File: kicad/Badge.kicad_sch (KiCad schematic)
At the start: 24 parts, among them SW1 SW_SPST, U1 LMC555xM

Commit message: outline draft 3
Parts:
- added C3: 100nF, Capacitor_SMD:C_0805_2012Metric_Pad1.18x1.45mm_HandSolder, symbol Device:C
- C1: value C -> 1uF
- R6, R7, R8, R9: value 470 -> 390
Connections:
- net GND: now also C3.2
- net VCC: now also C3.1
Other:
- note added: "3V 20mm coin cell CR2032 holder"
- note added: "LEDs"
- note added: "Power Supply"
- note added: "Timer"
- moved on the sheet: BT1, C1, C2, D1, D2, D3, D4, D5, D6, D7, D8, JP1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

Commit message: routing 1
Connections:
- net PULSE2L: now reaches JP2.2 (C), R6.2, R7.2, R8.2, R9.2
- net PULSE2H: now reaches D5.2 (A), D6.2 (A), D7.2 (A), D8.2 (A), JP1.2 (C)
- net BAT: now reaches BT1.1 (+), SW1.1 (A)
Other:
- company: (none) -> NJIT ECET 430
- title: (none) -> 430 Badge Solder Practice Board
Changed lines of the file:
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@@
 	(generator_version "8.0")
 	(paper "A4")
+	(title_block
+		(title "430 Badge Solder Practice Board")
+		(date "2024-10-02")
+		(rev "1.0")
+		(company "NJIT ECET 430")
+		(comment 1 "Open Source Hardware CC BY-NC-SA 4.0")
+	)
 	(junction
 		(at 219.71 48.26)
@@
 		)
 	)
+	(label "PULSE2L"
+		(at 232.41 85.09 270)
+		(fields_autoplaced yes)
+		(effects
+			(font
+				(size 1.27 1.27)
+				(thickness 0.1588)
+			)
+			(justify right bottom)
+		)
+	)
 	(label "PULSE"
 		(at 196.85 48.26 180)
@@
 		)
 	)
+	(label "BAT"
+		(at 27.94 53.34 0)
+		(fields_autoplaced yes)
+		(effects
+			(font
+				(size 1.27 1.27)
+				(thickness 0.254)
+				(bold yes)
+			)
+			(justify left bottom)
+		)
+	)
 	(label "TR"
 		(at 111.76 48.26 180)
@@
 		)
 	)
+	(label "PULSE2H"
+		(at 232.41 69.85 90)
+		(fields_autoplaced yes)
+		(effects
+			(font
+				(size 1.27 1.27)
+				(thickness 0.1588)
+			)
+			(justify left bottom)
+		)
+	)

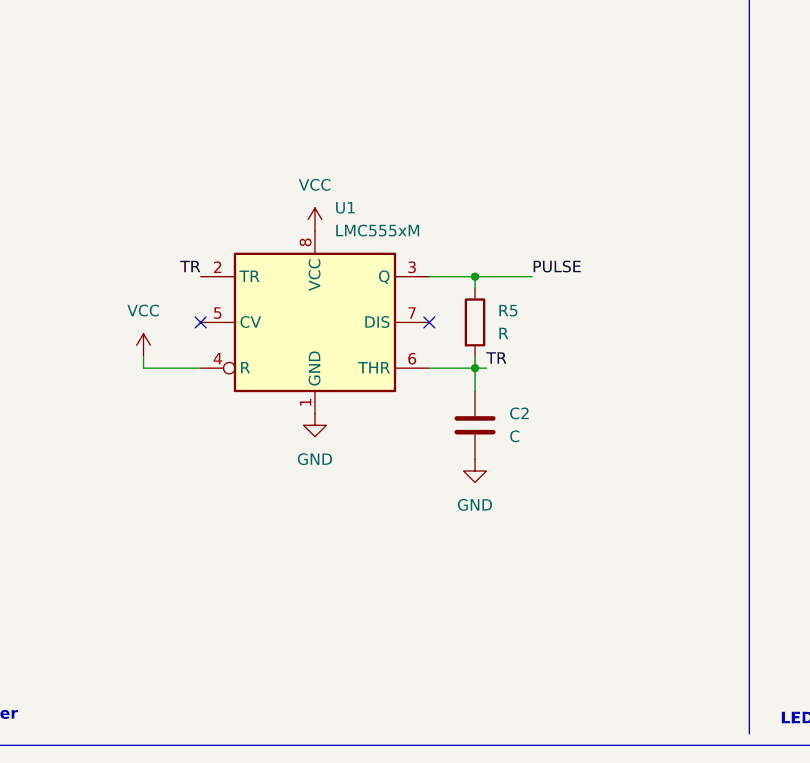
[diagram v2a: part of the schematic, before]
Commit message: fix routing, straight edge sections for solderpaste, milling gerbers
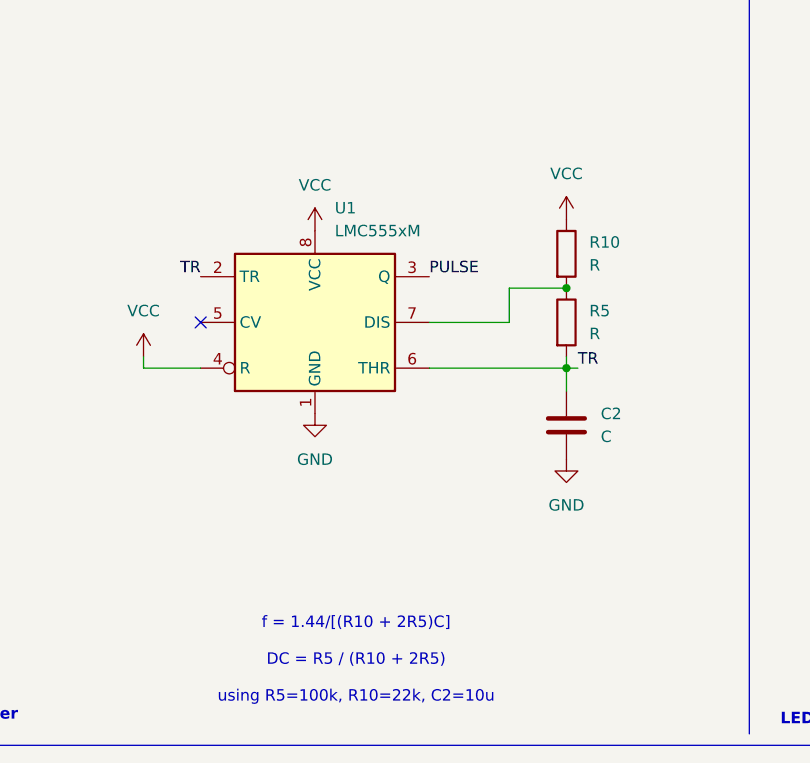
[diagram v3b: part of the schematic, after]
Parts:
- added R10: R, Resistor_SMD:R_0805_2012Metric_Pad1.20x1.40mm_HandSolder, symbol Device:R
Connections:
- net PULSE: no longer R5.1
- net VCC: now also R10.1
- net at U1.7 (DIS): now also R5.1, R10.2
- no-connect marks 2 -> 1
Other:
- note added: "f = 1.44/[(R10 + 2R5)C] DC = R5 / (R10 + 2R5) using R5=100k, R10=22k, C2=10u"
- moved on the sheet: C2, R5
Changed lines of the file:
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@@
 	)
 	(junction
-		(at 142.24 58.42)
+		(at 152.4 58.42)
 		(diameter 0)
 		(color 0 0 0 0)
@@
 	)
 	(junction
-		(at 142.24 48.26)
-		(diameter 0)
-		(color 0 0 0 0)
-	)
-	(junction
 		(at 48.26 63.5)
 		(diameter 0)
@@
 		(color 0 0 0 0)
 	)
-	(no_connect
-		(at 137.16 53.34)
+	(junction
+		(at 152.4 49.53)
+		(diameter 0)
+		(color 0 0 0 0)
 	)
 	(no_connect
@@
 	(wire
 		(pts
-			(xy 142.24 48.26) (xy 148.59 48.26)
-		)
-		(stroke
-			(width 0)
-			(type default)
-		)
-	)
-	(wire
-		(pts
-			(xy 137.16 48.26) (xy 142.24 48.26)
+			(xy 137.16 53.34) (xy 146.05 53.34)
+		)
+		(stroke
+			(width 0)
+			(type default)
+		)
+	)
+	(wire
+		(pts
+			(xy 146.05 49.53) (xy 152.4 49.53)
 		)
 		(stroke
@@
 	(wire
 		(pts
-			(xy 142.24 58.42) (xy 142.24 57.15)
+			(xy 152.4 58.42) (xy 152.4 57.15)
 		)
 		(stroke
@@
 	(wire
 		(pts
-			(xy 137.16 58.42) (xy 142.24 58.42)
+			(xy 137.16 58.42) (xy 152.4 58.42)
 		)
 		(stroke
@@
 	(wire
 		(pts
-			(xy 142.24 58.42) (xy 142.24 60.96)
+			(xy 152.4 58.42) (xy 152.4 60.96)
 		)
 		(stroke
@@
 	(wire
 		(pts
-			(xy 142.24 48.26) (xy 142.24 49.53)
-		)
-		(stroke
-			(width 0)
-			(type default)
-		)
-	)
-	(wire
-		(pts
 			(xy 105.41 58.42) (xy 105.41 57.15)
 		)
@@
 	(wire
 		(pts
+			(xy 146.05 53.34) (xy 146.05 49.53)
+		)
+		(stroke
+			(width 0)
+			(type default)
+		)
+	)
+	(wire
+		(pts
 			(xy 27.94 63.5) (xy 48.26 63.5)
 		)
@@
 	(wire
 		(pts
-			(xy 142.24 58.42) (xy 143.51 58.42)
+			(xy 152.4 58.42) (xy 153.67 58.42)
 		)
 		(stroke
@@
 		)
 	)
+	(text "f = 1.44/[(R10 + 2R5)C]\n\nDC = R5 / (R10 + 2R5)\n\nusing R5=100k, R10=22k, C2=10u"
+		(exclude_from_sim no)
+		(at 129.032 90.932 0)
+		(effects
+			(font
+				(size 1.27 1.27)
+			)
+		)
+	)
 	(text "3V 20mm coin cell\nCR2032 holder"
 		(exclude_from_sim no)
@@
 	)
 	(label "TR"
-		(at 143.51 58.42 0)
+		(at 153.67 58.42 0)
 		(fields_autoplaced yes)
 		(effects
@@
 	)
 	(label "PULSE"
-		(at 148.59 48.26 0)
+		(at 137.16 48.26 0)
 		(fields_autoplaced yes)
 		(effects
@@
 	(symbol
 		(lib_id "power:GND")
-		(at 142.24 68.58 0)
+		(at 152.4 68.58 0)
 		(unit 1)
 		(exclude_from_sim no)
@@
 		(fields_autoplaced yes)
 		(property "Reference" "#PWR06"
-			(at 142.24 74.93 0)
+			(at 152.4 74.93 0)
 			(effects
 				(font
@@
 		)
 		(property "Value" "GND"
-			(at 142.24 73.66 0)
+			(at 152.4 73.66 0)
 			(effects
 				(font
@@
 		)
 		(property "Footprint" ""
-			(at 142.24 68.58 0)
+			(at 152.4 68.58 0)
 			(effects
 				(font
@@
 		)
 		(property "Datasheet" ""
-			(at 142.24 68.58 0)
+			(at 152.4 68.58 0)
 			(effects
 				(font
@@
 		)
 		(property "Description" "Power symbol creates a global label with name \"GND\" , ground"
-			(at 142.24 68.58 0)
+			(at 152.4 68.58 0)
 			(effects
 				(font
@@
 	)
 	(symbol
+		(lib_id "power:VCC")
+		(at 152.4 41.91 0)
+		(unit 1)
+		(exclude_from_sim no)
+		(in_bom yes)
+		(on_board yes)
+		(dnp no)
+		(fields_autoplaced yes)
+		(property "Reference" "#PWR010"
+			(at 152.4 45.72 0)
+			(effects
+				(font
+					(size 1.27 1.27)
+				)
+				(hide yes)
+			)
+		)
+		(property "Value" "VCC"
+			(at 152.4 36.83 0)
+			(effects
+				(font
+					(size 1.27 1.27)
+				)
+			)
+		)
+		(property "Footprint" ""
+			(at 152.4 41.91 0)
+			(effects
+				(font
+					(size 1.27 1.27)
+				)
+				(hide yes)
+			)
+		)
+		(property "Datasheet" ""
+			(at 152.4 41.91 0)
+			(effects
+				(font
+					(size 1.27 1.27)
+				)
+				(hide yes)
+			)
+		)
+		(property "Description" "Power symbol creates a global label with name \"VCC\""
+			(at 152.4 41.91 0)
+			(effects
+				(font
+					(size 1.27 1.27)
+				)
+				(hide yes)
+			)
+		)
+		(pin "1"
+		)
+		(instances
+			(project "Badge"
+				(path "/e1b3ccd7-3caa-4d03-9727-c8afc9390c88"
+					(reference "#PWR010")
+					(unit 1)
+				)
+			)
+		)
+	)
+	(symbol
 		(lib_id "Switch:SW_SPST")
 		(at 38.1 53.34 0)
@@
 	)
 	(symbol
+		(lib_id "Device:R")
+		(at 152.4 45.72 0)
+		(unit 1)
+		(exclude_from_sim no)
+		(in_bom yes)
+		(on_board yes)
+		(dnp no)
+		(fields_autoplaced yes)
+		(property "Reference" "R10"
+			(at 154.94 44.4499 0)
+			(effects
+				(font
+					(size 1.27 1.27)
+				)
+				(justify left)
+			)
+		)
+		(property "Value" "R"
+			(at 154.94 46.9899 0)
+			(effects
+				(font
+					(size 1.27 1.27)
+				)
+				(justify left)
+			)
+		)
+		(property "Footprint" "Resistor_SMD:R_0805_2012Metric_Pad1.20x1.40mm_HandSolder"
+			(at 150.622 45.72 90)
+			(effects
+				(font
+					(size 1.27 1.27)
+				)
+				(hide yes)
+			)
+		)
+		(property "Datasheet" "~"
+			(at 152.4 45.72 0)
+			(effects
+				(font
+					(size 1.27 1.27)
+				)
+				(hide yes)
+			)
+		)
+		(property "Description" "Resistor"
+			(at 152.4 45.72 0)
+			(effects
+				(font
+					(size 1.27 1.27)
+				)
+				(hide yes)
+			)
+		)
+		(pin "1"
+		)
+		(pin "2"
+		)
+		(instances
+			(project "Badge"
+				(path "/e1b3ccd7-3caa-4d03-9727-c8afc9390c88"
+					(reference "R10")
+					(unit 1)
+				)
+			)
+		)
+	)
+	(symbol
 		(lib_id "Device:C")
 		(at 48.26 58.42 0)
@@
 	(symbol
 		(lib_id "Device:R")
-		(at 142.24 53.34 0)
+		(at 152.4 53.34 0)
 		(unit 1)
 		(exclude_from_sim no)
@@
 		(fields_autoplaced yes)
 		(property "Reference" "R5"
-			(at 144.78 52.0699 0)
+			(at 154.94 52.0699 0)
 			(effects
 				(font
@@
 		)
 		(property "Value" "R"
-			(at 144.78 54.6099 0)
+			(at 154.94 54.6099 0)
 			(effects
 				(font
@@
 		)
 		(property "Footprint" "Resistor_SMD:R_0805_2012Metric_Pad1.20x1.40mm_HandSolder"
-			(at 140.462 53.34 90)
+			(at 150.622 53.34 90)
 			(effects
 				(font
@@
 		)
 		(property "Datasheet" "~"
-			(at 142.24 53.34 0)
+			(at 152.4 53.34 0)
 			(effects
 				(font
@@
 		)
 		(property "Description" "Resistor"
-			(at 142.24 53.34 0)
+			(at 152.4 53.34 0)
 			(effects
 				(font
@@
 	(symbol
 		(lib_id "Device:C")
-		(at 142.24 64.77 0)
+		(at 152.4 64.77 0)
 		(unit 1)
 		(exclude_from_sim no)
@@
 		(fields_autoplaced yes)
 		(property "Reference" "C2"
-			(at 146.05 63.4999 0)
+			(at 156.21 63.4999 0)
 			(effects
 				(font
@@
 		)
 		(property "Value" "C"
-			(at 146.05 66.0399 0)
+			(at 156.21 66.0399 0)
 			(effects
 				(font
@@
 		)
 		(property "Footprint" "Capacitor_SMD:C_0805_2012Metric_Pad1.18x1.45mm_HandSolder"
-			(at 143.2052 68.58 0)
+			(at 153.3652 68.58 0)
 			(effects
 				(font
@@
 		)
 		(property "Datasheet" "~"
-			(at 142.24 64.77 0)
+			(at 152.4 64.77 0)
 			(effects
 				(font
@@
 		)
 		(property "Description" "Unpolarized capacitor"
-			(at 142.24 64.77 0)
-			(effects
-				(font
+			(at 152.4 64.77 0)
+			(effects
+				(font

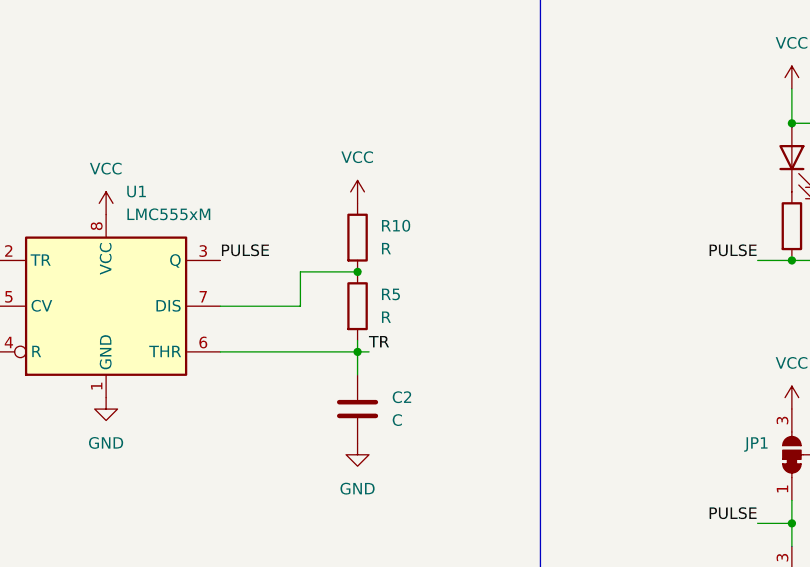
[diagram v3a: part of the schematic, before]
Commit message: fix discrepancies with milled board, to be milled again
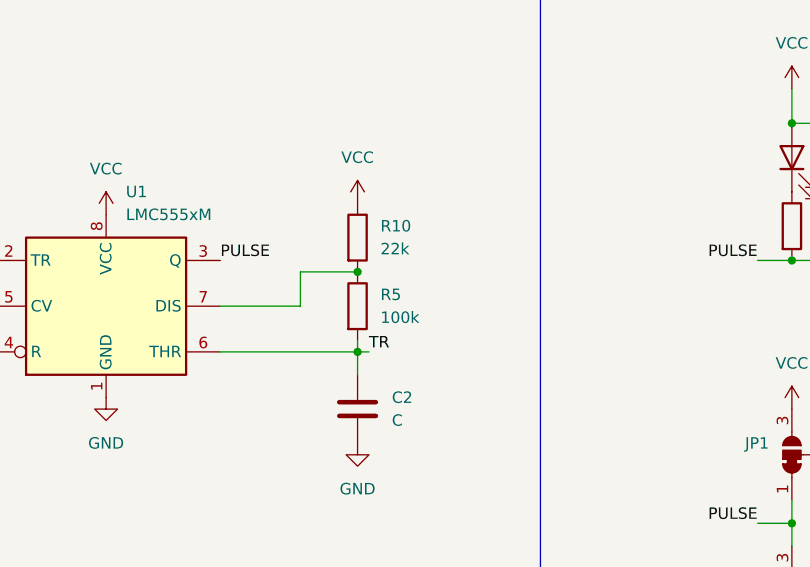
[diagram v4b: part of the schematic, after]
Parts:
- R10: value R -> 22k
- R5: value R -> 100k
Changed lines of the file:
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@@
 			)
 		)
-		(property "Value" "R"
+		(property "Value" "22k"
 			(at 154.94 46.9899 0)
 			(effects
@@
 			)
 		)
-		(property "Value" "R"
+		(property "Value" "100k"
 			(at 154.94 54.6099 0)
 			(effects

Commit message: 230 refactor
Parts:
- BT1: MFR (none) -> Keystone; MPN (none) -> 36-103-ND
- C1: value 1uF -> 10uF; MFR (none) -> generic; MPN (none) -> CAP CER 10UF 16V 0805
- C2: value C -> 10uF; MFR (none) -> generic; MPN (none) -> CAP CER 10UF 16V 0805
- C3: MFR (none) -> generic; MPN (none) -> CAP CER 0.1UF 25V 0805
- D1, D2, D3, D4: MFR (none) -> QTB; MPN (none) -> QBLP631-R5-2897
- D5, D6, D7, D8: MFR (none) -> QTB; MPN (none) -> QBLP631-AG1
- R1, R2, R3, R4: MPN (none) -> RES 470 OHM 1/8W 0805
- R10: MPN (none) -> RES 22K OHM 1/8W 0805
- R5: MPN (none) -> RES 100K OHM 1/8W 0805
- R6, R7, R8, R9: MPN (none) -> RES 390 OHM 1/8W 0805
- SW1: MFR (none) -> CUI; MPN (none) -> DS01-254-L-01BE
- U1: MFR (none) -> TI; MPN (none) -> LMC555CMX/NOPB
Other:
- note added: "390 or 470, try"
- company: NJIT ECET 430 -> NJIT ECET 230
- title: 430 Badge Solder Practice Board -> 230 Badge Solder Practice Board
- moved on the sheet: C3
